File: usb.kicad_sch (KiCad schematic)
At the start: 39 parts, among them J10 Conn_01x06_Pin, J2 Conn_ARM_SWD_TagConnect_TC2030, J4 Screw_Terminal_01x02, J5 Screw_Terminal_01x02, J6 Screw_Terminal_01x03, J7 Screw_Terminal_01x02, J8 Conn_01x06_Pin, J9 Conn_01x06_Pin, Q3 LMBT3906DW1T1G, Q4 AO3401A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

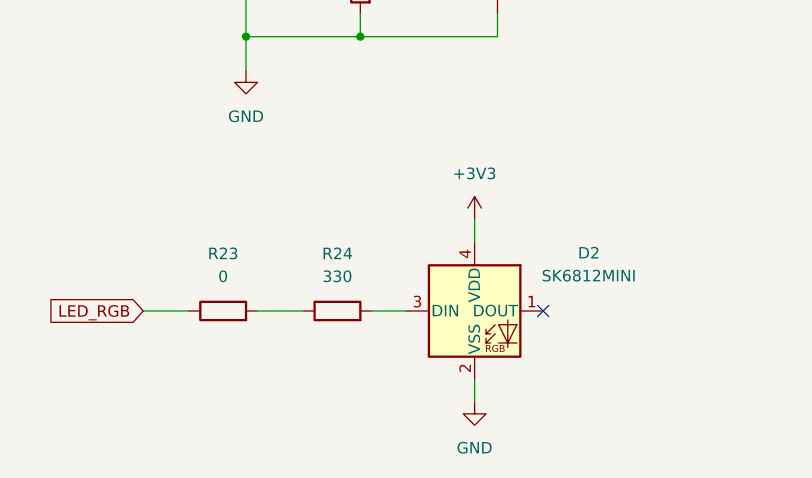
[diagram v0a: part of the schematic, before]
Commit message: footprints added, pcb started
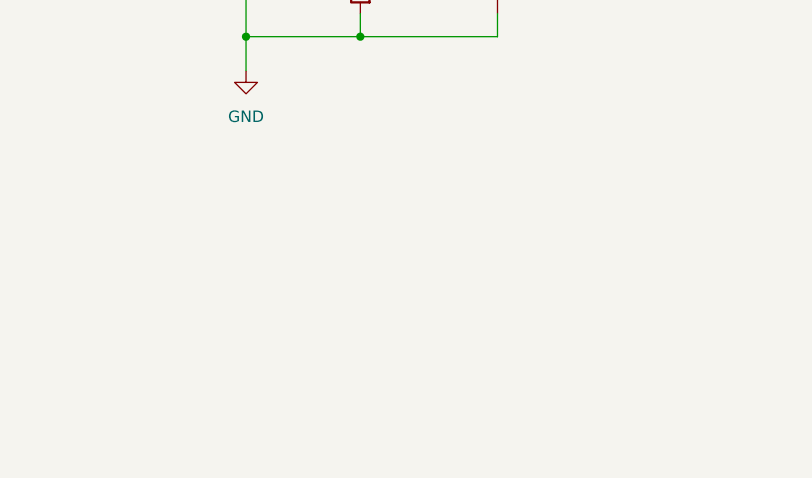
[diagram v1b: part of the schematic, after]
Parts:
- removed D2: SK6812MINI, LED_SMD:LED_SK6812MINI_PLCC4_3.5x3.5mm_P1.75mm, symbol LED:SK6812MINI
- removed R23: 0, PCM_JLCPCB:R_1206, symbol Device:R
- removed R24: 330, PCM_JLCPCB:R_0603, symbol Device:R
- J4, J5, J7: footprint (none) -> markus:DG305-5.0-02P-12-00A(H)
- J6: footprint (none) -> markus:DG305-5.0-03P-12-00A(H)
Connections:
- no-connect marks 2 -> 1

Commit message: before removing footprints
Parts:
- J7: now left out of the parts list
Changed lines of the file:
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@@
 		(body_style 1)
 		(exclude_from_sim no)
-		(in_bom yes)
+		(in_bom no)
 		(on_board yes)
 		(in_pos_files yes)
